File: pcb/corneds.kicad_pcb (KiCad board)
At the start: 2 copper layers, 320 x 105.6 mm, 120 parts, among them J3 AudioJack4, J4 AudioJack4, SW1 SW_Push, SW10 SW_Push, SW11 SW_Push, SW12 SW_Push, SW13 SW_Push, SW14 SW_Push, SW15 SW_Push, SW16 SW_Push, SW17 SW_Push, SW18 SW_Push, SW19 SW_Push, SW2 SW_Push, SW20 SW_Push, SW21 SW_Push, SW22 SW_Push, SW23 SW_Push, SW24 SW_Push, SW25 SW_Push, SW26 SW_Push, SW27 SW_Push, SW28 SW_Push, SW29 SW_Push, SW3 SW_Push, SW30 SW_Push, SW31 SW_Push, SW32 SW_Push, SW33 SW_Push, SW34 SW_Push, SW35 SW_Push, SW36 SW_Push, SW37 SW_Push, SW38 SW_Push, SW39 SW_Push, SW4 SW_Push, SW40 SW_Push, SW41 SW_Push, SW42 SW_Push, SW5 SW_Push, SW6 SW_Push, SW7 SW_Push, SW8 SW_Push, SW9 SW_Push, U1 Pico, U2 Pico, U3 SWD_Connector_3pin, U4 SWD_Connector_3pin, U5 Debug_UART_l, U6 Debug_UART_r

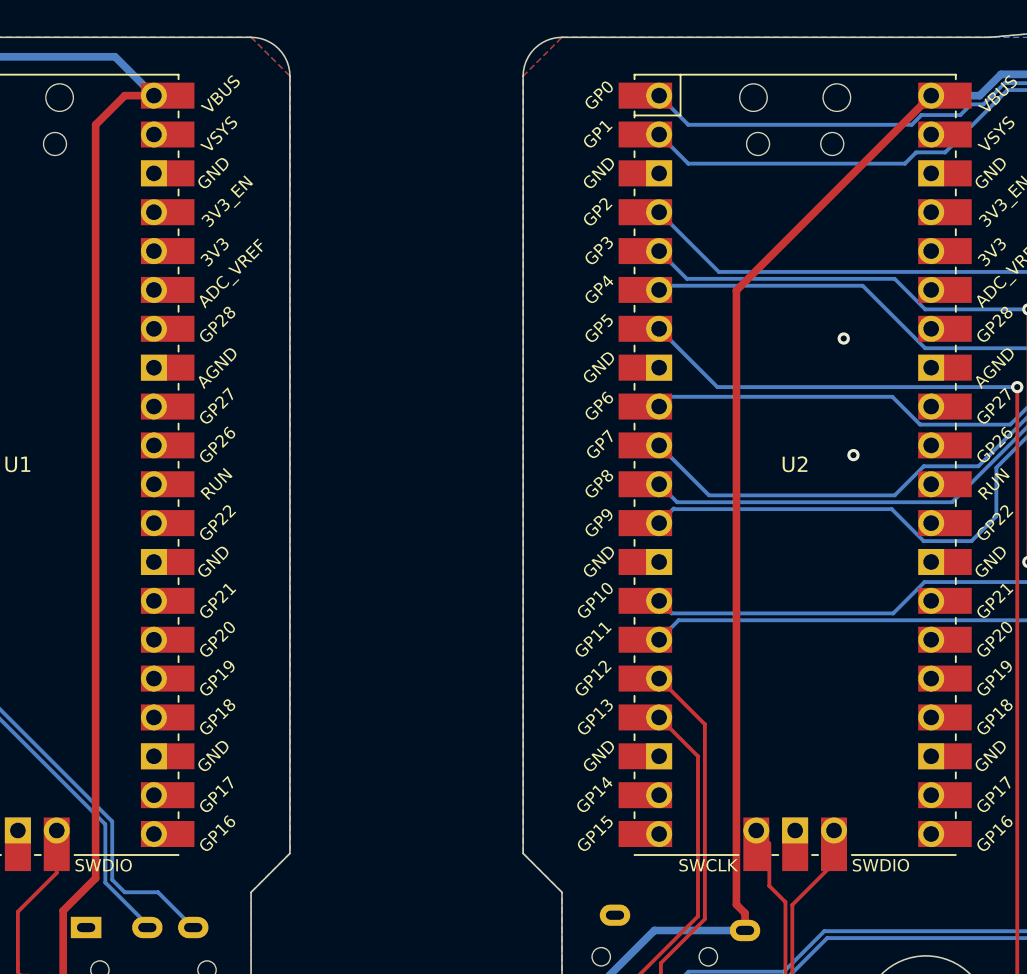
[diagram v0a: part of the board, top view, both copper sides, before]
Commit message: made led utils to have better readability over led states and switched board power to VSYS so we can differentiate right from left based on VBUS. This will run the peripheral board at 4.8V instead of 5V due to going through two schottky diodes
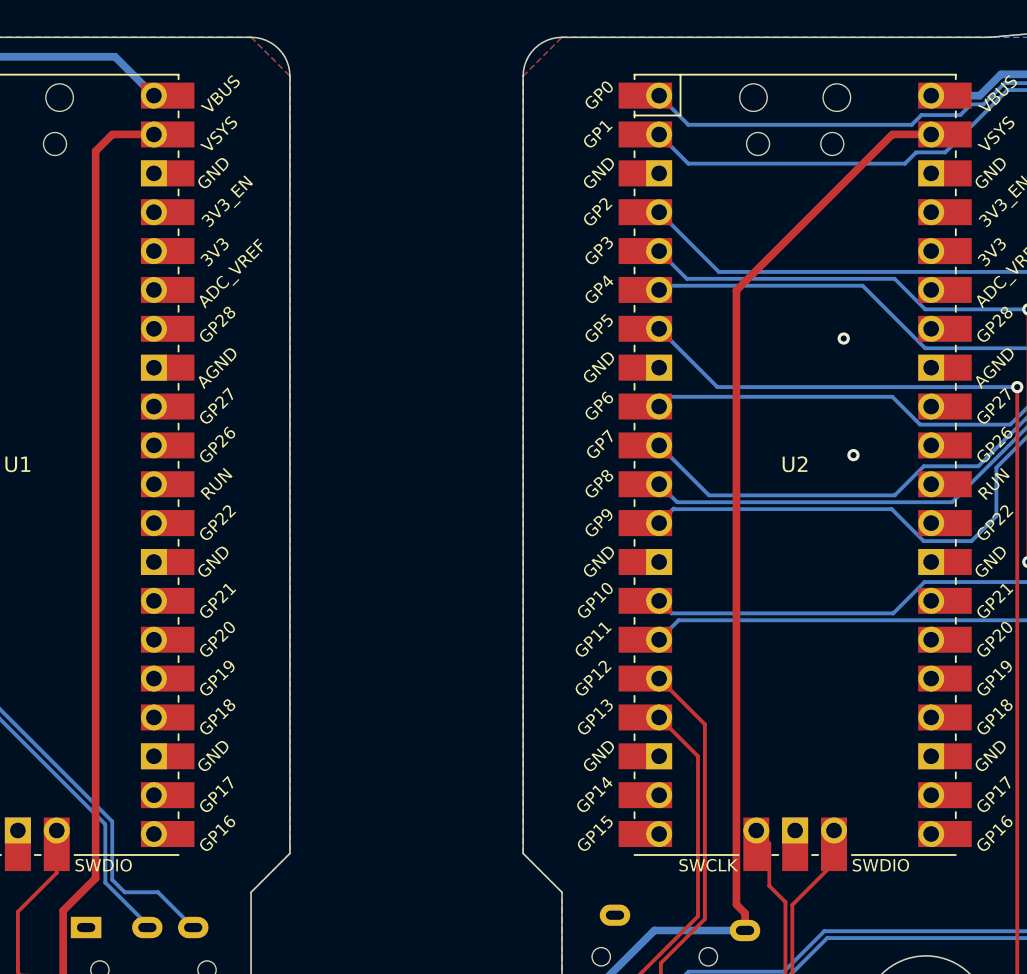
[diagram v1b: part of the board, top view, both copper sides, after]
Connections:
- U1 pad 39: unconnected-(U1-VSYS-Pad39) -> /vcc_l
- U1 pad 40: /vcc_l -> unconnected-(U1-VBUS-Pad40)
- U2 pad 39: unconnected-(U2-VSYS-Pad39) -> /vcc_r
- U2 pad 40: /vcc_r -> unconnected-(U2-VBUS-Pad40)
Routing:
- net /vcc_l: track 281.9 -> 279.8 mm
- net /vcc_r: track 282.5 -> 281.4 mm
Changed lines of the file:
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@@
   (net 94 "unconnected-(U1-3V3-Pad36)")
   (net 95 "unconnected-(U1-3V3_EN-Pad37)")
-  (net 96 "unconnected-(U1-VSYS-Pad39)")
+  (net 96 "unconnected-(U1-VBUS-Pad40)")
   (net 97 "unconnected-(U2-GPIO14-Pad19)")
   (net 98 "unconnected-(U2-GPIO15-Pad20)")
@@
   (net 112 "unconnected-(U2-3V3-Pad36)")
   (net 113 "unconnected-(U2-3V3_EN-Pad37)")
-  (net 114 "unconnected-(U2-VSYS-Pad39)")
+  (net 114 "unconnected-(U2-VBUS-Pad40)")
   (net 115 "unconnected-(U5-Pad3)")
   (net 116 "unconnected-(U5-Pad6)")
@@
       (net 61 "/gnd_r") (pinfunction "GND") (pintype "bidirectional"))
     (pad "39" thru_hole oval (at 8.89 -21.59) (size 1.7 1.7) (drill 1.02) (layers "*.Cu" "*.Mask")
-      (net 114 "unconnected-(U2-VSYS-Pad39)") (pinfunction "VSYS") (pintype "power_in"))
+      (net 57 "/vcc_r") (pinfunction "VSYS") (pintype "power_in"))
     (pad "39" smd rect (at 8.89 -21.59) (size 3.5 1.7) (drill (offset 0.9 0)) (layers "F.Cu" "F.Mask")
-      (net 114 "unconnected-(U2-VSYS-Pad39)") (pinfunction "VSYS") (pintype "power_in"))
+      (net 57 "/vcc_r") (pinfunction "VSYS") (pintype "power_in"))
     (pad "40" thru_hole oval (at 8.89 -24.13) (size 1.7 1.7) (drill 1.02) (layers "*.Cu" "*.Mask")
-      (net 57 "/vcc_r") (pinfunction "VBUS") (pintype "power_in"))
+      (net 114 "unconnected-(U2-VBUS-Pad40)") (pinfunction "VBUS") (pintype "power_in"))
     (pad "40" smd rect (at 8.89 -24.13) (size 3.5 1.7) (drill (offset 0.9 0)) (layers "F.Cu" "F.Mask")
-      (net 57 "/vcc_r") (pinfunction "VBUS") (pintype "power_in"))
+      (net 114 "unconnected-(U2-VBUS-Pad40)") (pinfunction "VBUS") (pintype "power_in"))
     (pad "41" thru_hole oval (at -2.54 23.9) (size 1.7 1.7) (drill 1.02) (layers "*.Cu" "*.Mask")
       (net 60 "/swclk_r") (pinfunction "SWCLK") (pintype "input"))
@@
       (net 55 "/gnd_l") (pinfunction "GND") (pintype "bidirectional"))
     (pad "39" thru_hole oval (at 8.89 -21.59) (size 1.7 1.7) (drill 1.02) (layers "*.Cu" "*.Mask")
-      (net 96 "unconnected-(U1-VSYS-Pad39)") (pinfunction "VSYS") (pintype "power_in"))
+      (net 51 "/vcc_l") (pinfunction "VSYS") (pintype "power_in"))
     (pad "39" smd rect (at 8.89 -21.59) (size 3.5 1.7) (drill (offset 0.9 0)) (layers "F.Cu" "F.Mask")
-      (net 96 "unconnected-(U1-VSYS-Pad39)") (pinfunction "VSYS") (pintype "power_in"))
+      (net 51 "/vcc_l") (pinfunction "VSYS") (pintype "power_in"))
     (pad "40" thru_hole oval (at 8.89 -24.13) (size 1.7 1.7) (drill 1.02) (layers "*.Cu" "*.Mask")
-      (net 51 "/vcc_l") (pinfunction "VBUS") (pintype "power_in"))
+      (net 96 "unconnected-(U1-VBUS-Pad40)") (pinfunction "VBUS") (pintype "power_in"))
     (pad "40" smd rect (at 8.89 -24.13) (size 3.5 1.7) (drill (offset 0.9 0)) (layers "F.Cu" "F.Mask")
-      (net 51 "/vcc_l") (pinfunction "VBUS") (pintype "power_in"))
+      (net 96 "unconnected-(U1-VBUS-Pad40)") (pinfunction "VBUS") (pintype "power_in"))
     (pad "41" thru_hole oval (at -2.54 23.9) (size 1.7 1.7) (drill 1.02) (layers "*.Cu" "*.Mask")
       (net 54 "/swclk_l") (pinfunction "SWCLK") (pintype "input"))
@@
   (segment (start 179.395357 109.357848) (end 181.10378 107.649425) (width 0.25) (layer "B.Cu") (net 50))
   (segment (start 176.824705 109.357848) (end 179.395357 109.357848) (width 0.25) (layer "B.Cu") (net 50))
-  (segment (start 122.34 100.78) (end 122.34 95.18) (width 0.5) (layer "F.Cu") (net 51))
-  (segment (start 124.46 93.06) (end 124.46 43.815) (width 0.5) (layer "F.Cu") (net 51))
-  (segment (start 124.46 43.815) (end 126.365 41.91) (width 0.5) (layer "F.Cu") (net 51))
-  (segment (start 126.365 41.91) (end 128.27 41.91) (width 0.5) (layer "F.Cu") (net 51))
+  (segment (start 124.46 45.54) (end 125.55 44.45) (width 0.5) (layer "F.Cu") (net 51))
+  (segment (start 125.55 44.45) (end 128.27 44.45) (width 0.5) (layer "F.Cu") (net 51))
   (segment (start 122.34 95.18) (end 124.46 93.06) (width 0.5) (layer "F.Cu") (net 51))
+  (segment (start 122.34 100.78) (end 122.34 95.18) (width 0.5) (layer "F.Cu") (net 51))
+  (segment (start 124.46 93.06) (end 124.46 45.54) (width 0.5) (layer "F.Cu") (net 51))
   (segment (start 10.795 47.625) (end 10.828696 47.658696) (width 0.5) (layer "B.Cu") (net 51))
   (segment (start 96.883172 100.78) (end 77.655 100.78) (width 0.5) (layer "B.Cu") (net 51))
@@
   (segment (start 80.831396 53.525) (end 64.321396 53.525) (width 0.25) (layer "B.Cu") (net 56))
   (segment (start 24.315 53.525) (end 20.955 50.165) (width 0.25) (layer "B.Cu") (net 56))
-  (segment (start 166.34 54.64) (end 179.07 41.91) (width 0.5) (layer "F.Cu") (net 57))
+  (segment (start 176.53 44.45) (end 179.07 44.45) (width 0.5) (layer "F.Cu") (net 57))
   (segment (start 166.34 94.785) (end 166.34 54.64) (width 0.5) (layer "F.Cu") (net 57))
   (segment (start 166.905 96.4725) (end 166.905 95.35) (width 0.5) (layer "F.Cu") (net 57))
+  (segment (start 166.34 54.64) (end 176.53 44.45) (width 0.5) (layer "F.Cu") (net 57))
   (segment (start 166.905 95.35) (end 166.34 94.785) (width 0.5) (layer "F.Cu") (net 57))
   (segment (start 156.845 103.505) (end 158.75 105.41) (width 0.5) (layer "B.Cu") (net 57))

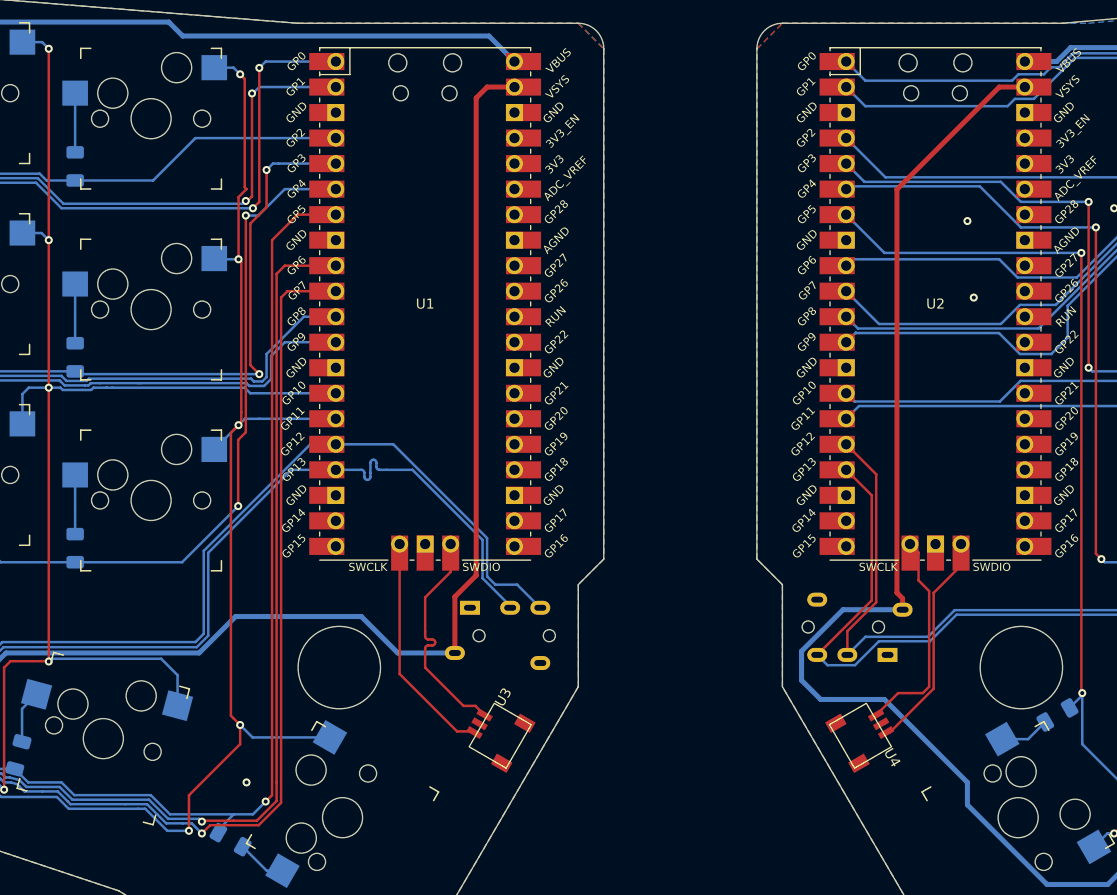
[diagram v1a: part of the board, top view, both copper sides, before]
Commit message: dbg_uart and xboard_uart were both uart0 so I swapped dbg_uart with cols 0 and 1
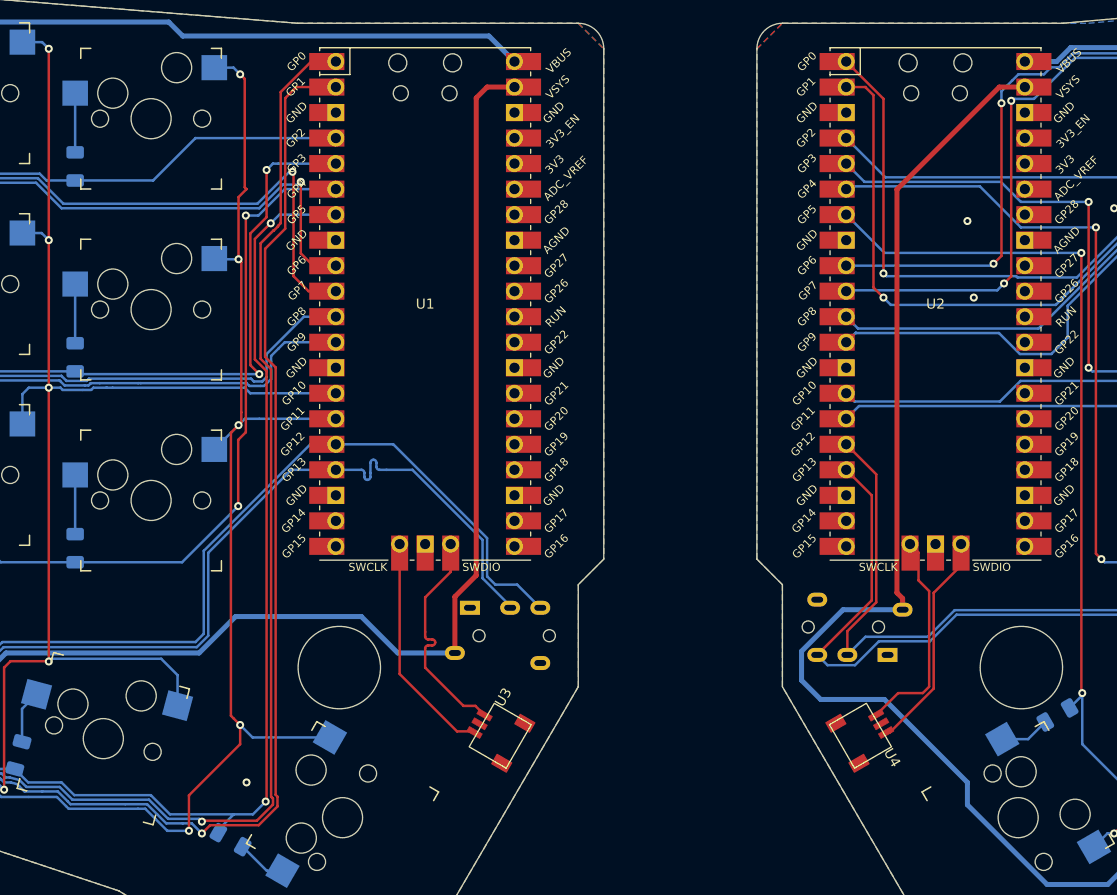
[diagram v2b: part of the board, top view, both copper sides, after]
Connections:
- U1 pad 1: /dbg_uart_tx_l -> /col0_l
- U1 pad 10: /col1_l -> /dbg_uart_rx_l
- U1 pad 2: /dbg_uart_rx_l -> /col1_l
- U1 pad 9: /col0_l -> /dbg_uart_tx_l
- U2 pad 1: /dbg_uart_tx_r -> /col0_r
- U2 pad 10: /col1_r -> /dbg_uart_rx_r
- U2 pad 2: /dbg_uart_rx_r -> /col1_r
- U2 pad 9: /col0_r -> /dbg_uart_tx_r
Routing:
- net /col1_l: track 220.2 -> 241.1 mm
- net /col0_l: track 220.9 -> 240.8 mm
- net /col0_r: track 242.7 -> 260.7 mm, vias 0 -> 1
- net /col1_r: track 210.7 -> 228.8 mm, vias 3 -> 4
- net /dbg_uart_tx_r: track 133.2 -> 150.6 mm, vias 0 -> 2
- net /dbg_uart_rx_r: track 136.6 -> 153.7 mm, vias 0 -> 2
- net /dbg_uart_tx_l: track 114.3 -> 109.2 mm, vias 2 -> 1
- net /row3_l: track 147.4 -> 149.5 mm, vias 3 -> 4
- net /dbg_uart_rx_l: track 109.6 -> 111.0 mm, vias 2 -> 1

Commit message: updated to rev3 of the pcb
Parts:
- added R1: 100Ω, Resistor_SMD:R_0603_1608Metric, B.Cu at (165.1, 87.2)
- added R2: 100Ω, Resistor_SMD:R_0603_1608Metric, B.Cu at (101.6, 89.7)
- added Reset_l1: SW_Push, entropy:SW_PTS636_SK25F_SMTR, F.Cu at (103.4, 99.1)
- added Reset_r1: SW_Push, entropy:SW_PTS636_SK25F_SMTR, F.Cu at (186.2, 99.1)
- J3, J4: moved to F.Cu
- moved J4 5.47 mm to (165.4, 101.4), turned to 90 degrees
- moved J3 4.85 mm to (124.2, 96.5), turned to -90 degrees
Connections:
- U1 pad 10: /dbg_uart_rx_l -> /row3_l
- U1 pad 19: unconnected-(U1-GPIO14-Pad19) -> Net-(U1-GPIO14)
- U1 pad 30: unconnected-(U1-RUN-Pad30) -> Net-(U1-RUN)
- U1 pad 6: /row2_l -> /dbg_uart_tx_l
- U1 pad 7: /row3_l -> /dbg_uart_rx_l
- U1 pad 9: /dbg_uart_tx_l -> /row2_l
- U2 pad 10: /dbg_uart_rx_r -> /row3_r
- U2 pad 19: unconnected-(U2-GPIO14-Pad19) -> Net-(U2-GPIO14)
- U2 pad 30: unconnected-(U2-RUN-Pad30) -> Net-(U2-RUN)
- U2 pad 6: /row2_r -> /dbg_uart_tx_r
- U2 pad 7: /row3_r -> /dbg_uart_rx_r
- U2 pad 9: /dbg_uart_tx_r -> /row2_r
- U5 pad 2: /vcc_l -> unconnected-(U5-Pad2)
- U5 pad 3: unconnected-(U5-Pad3) -> /vcc_l
- U6 pad 2: /vcc_r -> unconnected-(U6-Pad2)
- U6 pad 3: unconnected-(U6-Pad3) -> /vcc_r
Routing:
- net Net-(U1-RUN): track 0.00 -> 51.1 mm, vias 0 -> 1
- net Net-(U2-RUN): track 0.00 -> 35.9 mm
- net /vcc_r: track 281.4 -> 269.2 mm
- net Net-(U1-GPIO14): track 0.00 -> 9.42 mm
- net /xboard_uart_rx_l: track 121.4 -> 127.1 mm
- net /xboard_uart_tx_r: track 102.9 -> 98.0 mm
- net /xboard_uart_tx_l: track 122.7 -> 126.9 mm
- net /xboard_uart_rx_r: track 110.5 -> 106.5 mm
- net Net-(U2-GPIO14): track 0.00 -> 3.97 mm
- net /col0_l: track 240.8 -> 237.7 mm
- net /row0_l: track 174.2 -> 176.8 mm
- net /col3_r: track 193.6 -> 195.1 mm
- net /dbg_uart_rx_r: track 153.7 -> 152.3 mm
- net /col5_l: track 176.5 -> 177.8 mm
- net /col2_r: track 190.2 -> 191.2 mm
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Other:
- outline, holes or cut-outs redrawn
- board text added: "21 Nov 2023"
- board text removed: "26 Apr 2023"
